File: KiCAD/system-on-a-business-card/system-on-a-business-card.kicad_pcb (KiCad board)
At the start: 4 copper layers, 85 x 54 mm, 83 parts, among them J1 USB_C_Receptacle, J2 X077-6428TSWCG01-H13, J3 Conn_01x04_Socket, Q1 2N7002K, Q2 2N7002K, SW1 SW_Push, SW2 SW_Push, U1 USBLC6-2SC6, U2 ESP32-C3, U3 ZD25WQ32C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

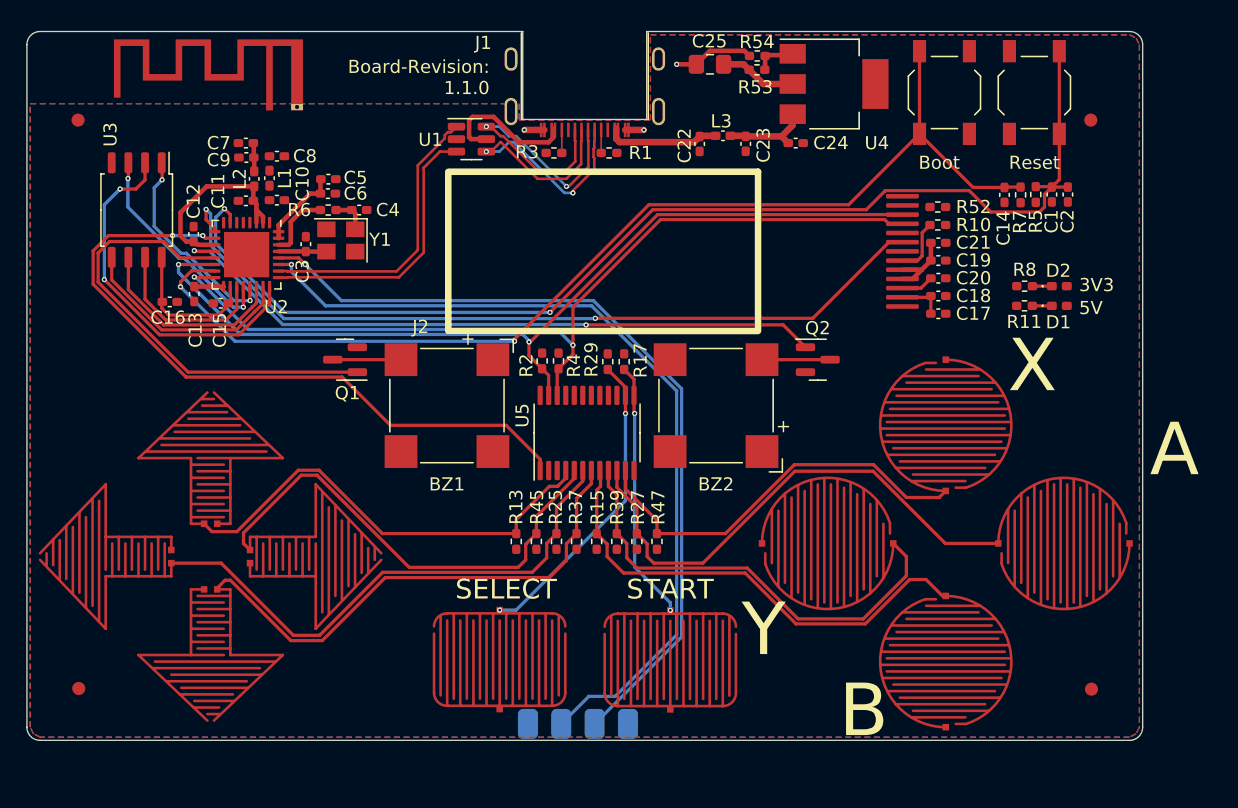
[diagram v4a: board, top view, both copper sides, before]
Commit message: #10: added micro sd card
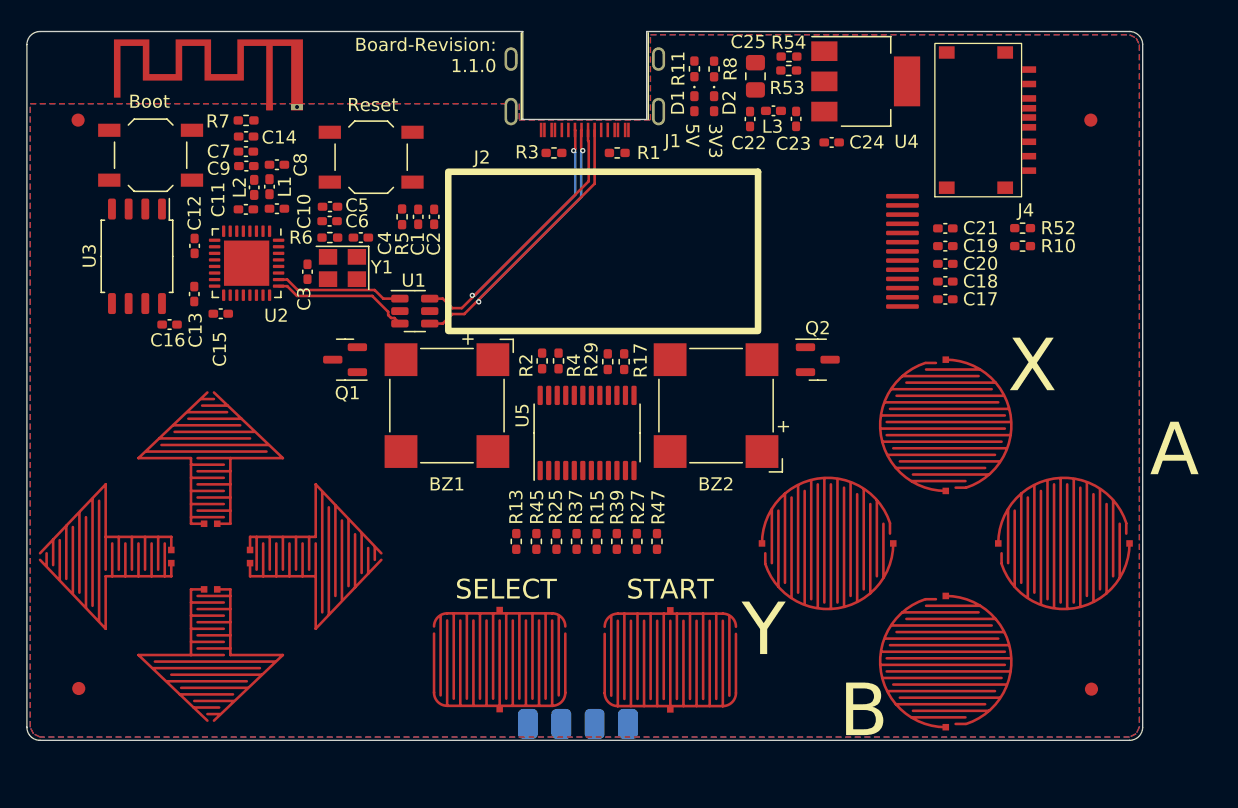
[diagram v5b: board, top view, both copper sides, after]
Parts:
- added J4: Micro_SD_Card, Prj_connector_card:microSD_HC_Hanbo_Electronic_TF-018B-H15, F.Cu at (153.3, 76.8)
- moved SW2 60.7 mm to (86.9, 79.4), turned to 0 degrees
- moved R7 59.3 mm to (94.2, 76.8), turned to 180 degrees
- moved C14 57.9 mm to (94.2, 78.0), turned to 0 degrees
- moved SW1 50.8 mm to (103.7, 79.6), turned to 180 degrees
- moved C1 48.3 mm to (107.3, 84.1)
- moved C2 48.3 mm to (108.5, 84.1)
- moved R5 48.3 mm to (106.1, 84.1)
- moved D1 31.8 mm to (128.3, 75.5), turned to -90 degrees
- moved R11 31.0 mm to (128.3, 72.8), turned to 90 degrees
- moved D2 29.7 mm to (129.8, 75.5), turned to -90 degrees
- moved R8 28.9 mm to (129.8, 72.9), turned to 90 degrees
- moved U1 13.8 mm to (107.0, 91.3)
- moved R10 6.66 mm to (153.4, 86.3)
- moved R52 6.66 mm to (153.4, 85.0)
- moved C23 4.28 mm to (136.1, 76.7)
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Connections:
- U2 pad 10: /Host/IO_EXP_INT -> MTDI
- U2 pad 12: BUZZER_R -> MTCK
- U2 pad 13: BUZZER_L -> MTDO
- U2 pad 4: unconnected-(U2-XTAL_32K_P/ADC1_CH0-Pad4) -> /Display Circuit/RESET_DISPLAY
- U2 pad 5: unconnected-(U2-XTAL_32K_N/ADC1_CH1-Pad5) -> /Host/IO_EXP_INT
- U2 pad 6: unconnected-(U2-GPIO2/ADC1_CH2-Pad6) -> BUZZER_R
- U2 pad 8: unconnected-(U2-GPIO3/ADC1_CH3-Pad8) -> BUZZER_L
- U2 pad 9: /Display Circuit/RESET_DISPLAY -> MTMS
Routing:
- net RESET: track 89.0 -> 0.00 mm, vias 2 -> 0
- net BOOT: track 83.7 -> 0.00 mm, vias 2 -> 0
- net /Display Circuit/SDA: track 69.5 -> 0.00 mm, vias 2 -> 0
- net /Display Circuit/SCL: track 67.8 -> 0.00 mm, vias 2 -> 0
- net UART_RXD: track 64.8 -> 0.00 mm, vias 1 -> 0
- net UART_TXD: track 63.1 -> 0.00 mm, vias 1 -> 0
- net /Display Circuit/RESET_DISPLAY: track 62.3 -> 0.00 mm, vias 2 -> 0
- net /Host/IO_EXP_INT: track 52.8 -> 0.00 mm, vias 2 -> 0
- net BUZZER_R: track 51.4 -> 0.00 mm, vias 2 -> 0
- net LEFT: track 41.1 -> 0.00 mm
- net A: track 39.6 -> 0.00 mm
- net DOWN: track 39.0 -> 0.00 mm
- net B: track 36.9 -> 0.00 mm
- net RIGHT: track 36.3 -> 0.00 mm
- net +3.3V: track 35.9 -> 0.00 mm
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
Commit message: #10: continued with routing
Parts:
- moved R15 1.53 mm to (122.4, 108.8)
- moved R39 1.53 mm to (120.9, 108.8)
- moved C13 0.94 mm to (90.3, 90.9)
- moved C12 0.78 mm to (89.5, 86.3)
- moved R1 0.42 mm to (122.0, 79.2)
- moved C25 0.07 mm to (133.0, 73.3)
- turned R38 to -90 degrees
- turned R7 to 0 degrees
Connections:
- U5 pad 8: B -> Y
- U5 pad 9: Y -> B
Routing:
- net +3.3V: track 0.00 -> 401.4 mm
- net MTMS: track 0.00 -> 81.0 mm, vias 0 -> 2
- net MTDO: track 0.00 -> 80.6 mm, vias 0 -> 2
- net MTCK: track 0.00 -> 80.1 mm, vias 0 -> 2
- net MTDI: track 0.00 -> 78.0 mm, vias 0 -> 2
- net /Display Circuit/SDA: track 0.00 -> 70.6 mm, vias 0 -> 3
- net /Display Circuit/SCL: track 0.00 -> 68.6 mm, vias 0 -> 3
- net B: track 0.00 -> 42.8 mm
- net A: track 0.00 -> 41.7 mm
- net LEFT: track 0.00 -> 41.0 mm
- net DOWN: track 0.00 -> 39.0 mm
- net UP: track 0.00 -> 38.1 mm
- net RIGHT: track 0.00 -> 37.3 mm
- net +5V: track 0.00 -> 32.7 mm
- net X: track 0.00 -> 32.2 mm
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- removed copper zone on In1.Cu, net GND
- removed copper zone on In2.Cu, net GND
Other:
- copper layers 4 -> 2

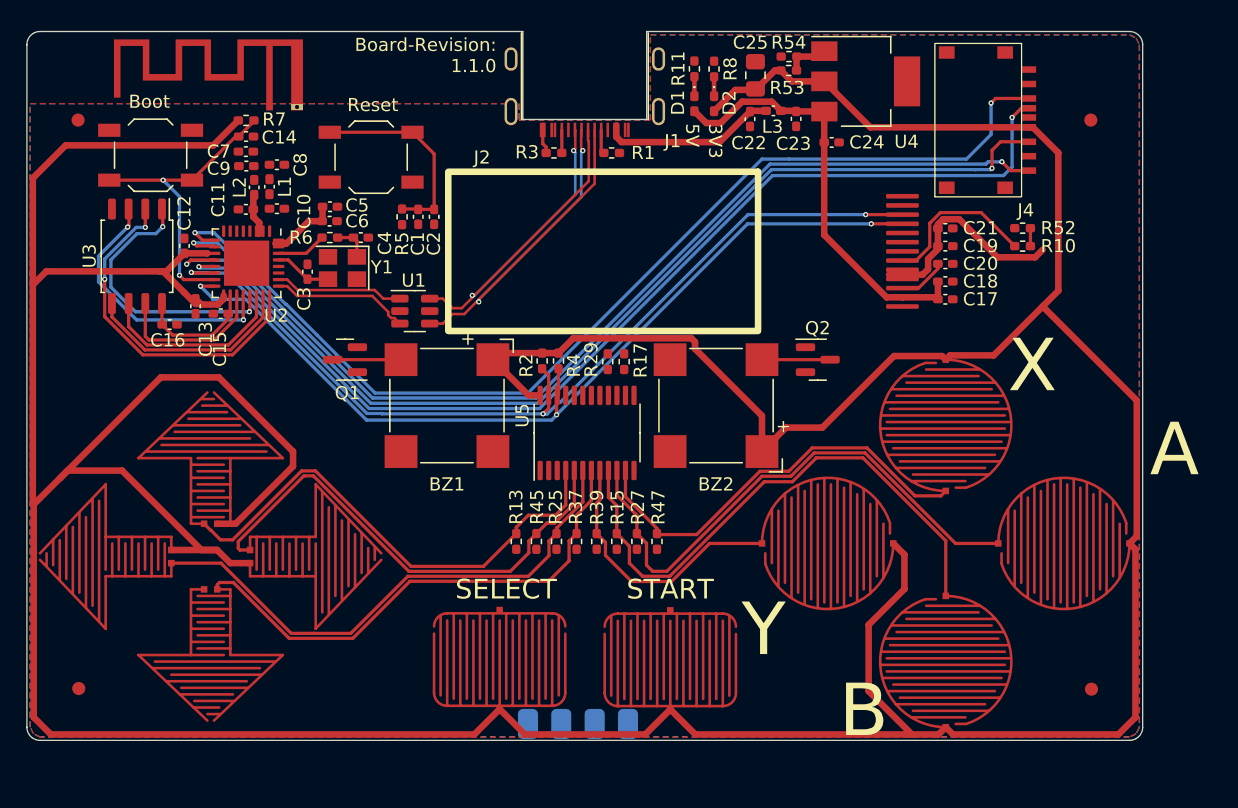
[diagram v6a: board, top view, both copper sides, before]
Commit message: #10: finished routing except PCB antenna
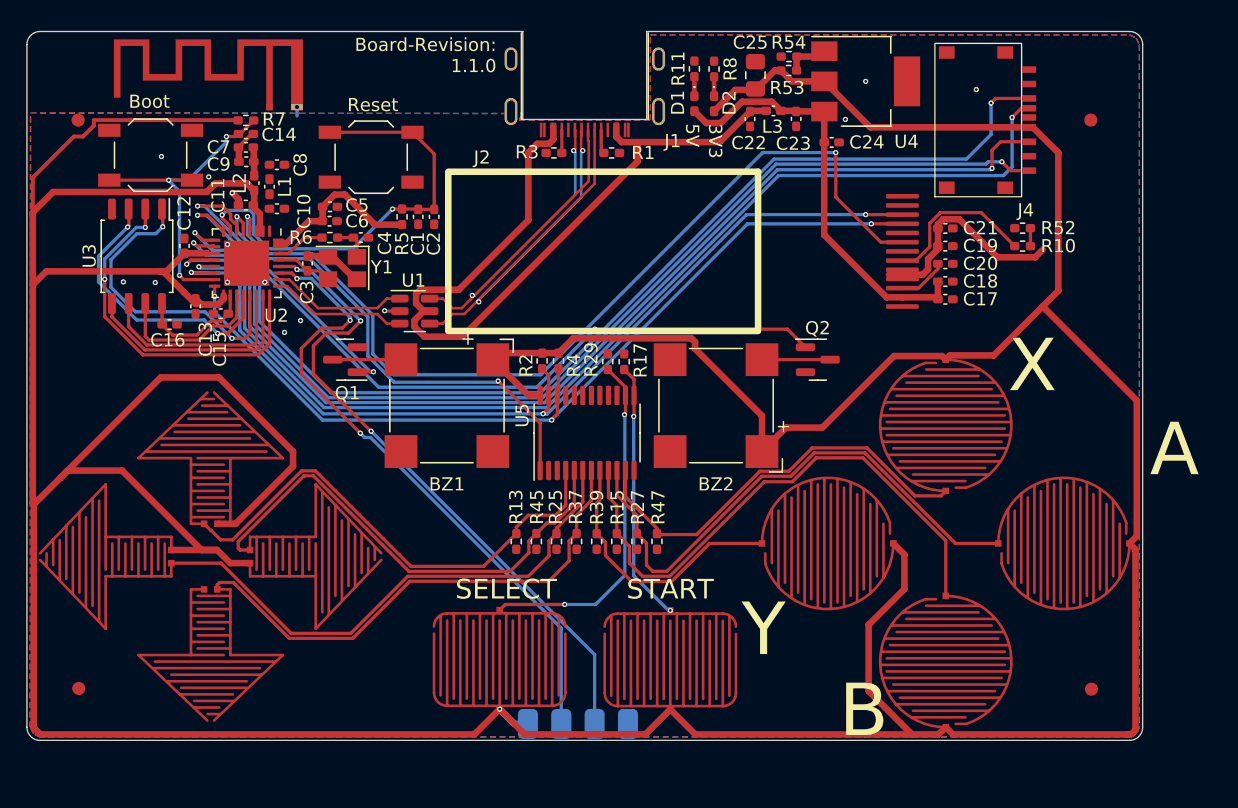
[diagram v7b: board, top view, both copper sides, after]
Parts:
- moved C3 0.63 mm to (98.9, 87.7)
- moved C11 0.33 mm to (94.2, 83.2)
- moved C7 0.33 mm to (94.2, 78.8)
- moved C9 0.33 mm to (94.2, 79.9)
- moved L2 0.33 mm to (94.8, 81.6)
- moved C14 0.20 mm to (94.2, 77.8)
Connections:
- U2 pad 6: BUZZER_R -> BUZZER_L
- U2 pad 8: BUZZER_L -> BUZZER_R
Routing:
- net /Display Circuit/RESET_DISPLAY: track 0.00 -> 70.5 mm, vias 0 -> 2
- net BUZZER_R: track 0.00 -> 56.6 mm, vias 0 -> 2
- net UART_TXD: track 0.00 -> 50.0 mm, vias 0 -> 3
- net UART_RXD: track 0.00 -> 48.7 mm, vias 0 -> 3
- net /Power Circuit/USB_VBUS: track 13.4 -> 60.6 mm
- net /Host/IO_EXP_INT: track 0.00 -> 37.0 mm, vias 0 -> 2
- net +3.3V: track 401.4 -> 431.2 mm, vias 0 -> 1
- net SELECT: track 0.00 -> 26.9 mm, vias 0 -> 2
- net BUZZER_L: track 0.00 -> 24.2 mm, vias 0 -> 2
- net START: track 0.00 -> 19.9 mm, vias 0 -> 2
- net RESET: track 15.3 -> 34.0 mm, vias 0 -> 2
- net GND: track 2.31 -> 10.1 mm, vias 0 -> 14
- net Net-(U2-SPICS0/GPIO14): track 21.1 -> 23.7 mm
- net Net-(C7-Pad1): track 0.00 -> 2.18 mm
- net /Display Circuit/SDA: track 70.6 -> 72.6 mm
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
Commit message: #10: finished initial routing
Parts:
- moved FID1 1.62 mm to (158.5, 78.4)
- moved FID3 0.85 mm to (81.5, 77.6)
- moved AE1 0.45 mm to (96.4, 75.8)
- moved C10 0.45 mm to (97.0, 83.5)
- moved C8 0.45 mm to (97.0, 80.2)
- moved L1 0.45 mm to (96.4, 81.8)
- moved C25 0.40 mm to (132.6, 73.3)
- moved J3 0.25 mm to (123.3, 122.5)
- moved BZ1 0.20 mm to (109.5, 98.7)
- moved Q1 0.20 mm to (101.7, 95.2)
- moved Q2 0.20 mm to (137.8, 95.2)
- moved C11 0.18 mm to (94.2, 83.4)
- moved L2 0.18 mm to (94.8, 81.7)
- moved C14 0.17 mm to (94.2, 78.0)
- moved C7 0.17 mm to (94.2, 79.0)
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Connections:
- J4 pad 9: unconnected-(J4-DET-Pad9) -> /Host/SDcard_DET
- U5 pad 15: unconnected-(U5-P12-Pad15) -> /Host/SDcard_DET
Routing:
- net /Host/SDcard_DET: track 0.00 -> 55.3 mm, vias 0 -> 2
- net +3.3V: track 431.2 -> 482.2 mm, vias 1 -> 3
- net GND: track 10.1 -> 24.9 mm, vias 14 -> 43
- net Net-(AE1-Feed): track 0.00 -> 4.60 mm
- net Net-(U2-LNA_IN): track 0.00 -> 2.49 mm
- net /Display Circuit/RESET_DISPLAY: track 70.5 -> 72.8 mm
- net RESET: track 34.0 -> 36.2 mm
- net Net-(U2-VDD_SPI/GPIO11): track 9.12 -> 10.9 mm
- net Net-(J2-Pin_6): track 12.2 -> 13.6 mm
- net /Host/IO_EXP_INT: track 37.0 -> 35.6 mm
- net /Power Circuit/USB_VBUS: track 60.6 -> 59.3 mm
- net Net-(U2-SPIWP/GPIO13): track 21.4 -> 22.5 mm
- net Net-(U2-SPIHD/GPIO12): track 12.0 -> 13.1 mm
- net /Display Circuit/SDA: track 72.6 -> 71.8 mm
- net Net-(U2-SPID/GPIO16): track 17.4 -> 18.1 mm
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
